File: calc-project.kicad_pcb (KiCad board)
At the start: 2 copper layers, 54 parts, among them J2 Conn_01x08_Socket, J3 Conn_01x08_Socket, J4 Conn_01x08_Socket, SW1 SW_Push_45deg, SW10 SW_Push_45deg, SW11 SW_Push_45deg, SW12 SW_Push_45deg, SW13 SW_Push_45deg, SW14 SW_Push_45deg, SW15 SW_Push_45deg, SW16 SW_Push_45deg, SW17 SW_Push_45deg, SW18 SW_Push_45deg, SW19 SW_Push_45deg, SW2 SW_Push_45deg, SW20 SW_Push_45deg, SW21 SW_Push_45deg, SW22 SW_Push_45deg, SW23 SW_Push_45deg, SW24 SW_Push_45deg, SW25 SW_Push_45deg, SW26 SW_Push_45deg, SW27 SW_Push_45deg, SW28 SW_Push_45deg, SW29 SW_Push_45deg, SW3 SW_Push_45deg, SW30 SW_Push_45deg, SW31 SW_Push_45deg, SW32 SW_Push_45deg, SW33 SW_Push_45deg, SW34 SW_Push_45deg, SW35 SW_Push_45deg, SW36 SW_Push_45deg, SW37 SW_Push_45deg, SW38 SW_Push_45deg, SW39 SW_Push_45deg, SW4 SW_Push_45deg, SW40 SW_Push_45deg, SW41 SW_Push_45deg, SW42 SW_Push_45deg, SW43 SW_Push_45deg, SW44 SW_Push_45deg, SW45 SW_Push_45deg, SW46 SW_Push_45deg, SW47 SW_Push_45deg, SW48 SW_Push_45deg, SW5 SW_Push_45deg, SW6 SW_Push_45deg, SW7 SW_Push_45deg, SW8 SW_Push_45deg, SW9 SW_Push_45deg

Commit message: added rpi pico, took away connectors, idk what else
idk what i did
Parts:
- added J1: PinSocket_1x20_Right, Connector_PinSocket_2.54mm:PinSocket_1x20_P2.54mm_Vertical_SMD_Pin1Left, B.Cu at (62.9, 68.0)
- added J2: PinSocket_1x20_Left, Connector_PinSocket_2.54mm:PinSocket_1x20_P2.54mm_Vertical_SMD_Pin1Left, B.Cu at (55.6, 68.0)
- moved SW43 76.2 mm to (133.0, 138.0), turned to 90 degrees
- moved SW48 75.6 mm to (133.0, 88.0), turned to 90 degrees
- moved SW44 70.7 mm to (133.0, 128.0), turned to 90 degrees
- moved SW47 70.2 mm to (133.0, 98.0), turned to 90 degrees
- moved SW45 67.6 mm to (133.0, 118.0), turned to 90 degrees
- moved SW46 67.5 mm to (133.0, 108.0), turned to 90 degrees
- moved SW37 65.3 mm to (124.0, 138.0), turned to 90 degrees
- moved SW42 64.5 mm to (124.0, 88.0), turned to 90 degrees
- moved J2 58.7 mm to (101.0, 74.0), turned to 90 degrees
- moved SW38 58.7 mm to (124.0, 128.0), turned to 90 degrees
- moved SW41 58.2 mm to (124.0, 98.0), turned to 90 degrees
- moved SW39 55.0 mm to (124.0, 118.0), turned to 90 degrees
- moved SW40 54.8 mm to (124.0, 108.0), turned to 90 degrees
- moved SW31 54.1 mm to (114.0, 138.0), turned to 90 degrees
- moved SW36 53.2 mm to (114.0, 88.0), turned to 90 degrees
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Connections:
- LCD1 pad 10: Net-(J3-Pin_4) -> unconnected-(LCD1-~{CSX}-Pad10)
- LCD1 pad 11: Net-(J3-Pin_3) -> unconnected-(LCD1-DCX-Pad11)
- LCD1 pad 12: Net-(J3-Pin_2) -> unconnected-(LCD1-WRX-Pad12)
- LCD1 pad 33: Net-(J3-Pin_1) -> unconnected-(LCD1-SDA-Pad33)
- SW1 pad 1: Net-(J4-Pin_8) -> Net-(SW1-Pad1)
- SW1 pad 2: Net-(J2-Pin_8) -> Net-(SW1-Pad2)
- SW10 pad 1: Net-(J4-Pin_5) -> Net-(SW10-Pad1)
- SW10 pad 2: Net-(J2-Pin_7) -> Net-(SW10-Pad2)
- SW11 pad 1: Net-(J4-Pin_4) -> Net-(SW11-Pad1)
- SW11 pad 2: Net-(J2-Pin_7) -> Net-(SW10-Pad2)
- SW12 pad 1: Net-(J4-Pin_3) -> Net-(SW12-Pad1)
- SW12 pad 2: Net-(J2-Pin_7) -> Net-(SW10-Pad2)
- SW13 pad 1: Net-(J4-Pin_8) -> Net-(SW1-Pad1)
- SW13 pad 2: Net-(J2-Pin_6) -> Net-(SW13-Pad2)
- SW14 pad 1: Net-(J4-Pin_7) -> Net-(SW14-Pad1)
- SW14 pad 2: Net-(J2-Pin_6) -> Net-(SW13-Pad2)
- SW15 pad 1: Net-(J4-Pin_6) -> Net-(SW15-Pad1)
- SW15 pad 2: Net-(J2-Pin_6) -> Net-(SW13-Pad2)
- SW16 pad 1: Net-(J4-Pin_5) -> Net-(SW10-Pad1)
- SW16 pad 2: Net-(J2-Pin_6) -> Net-(SW13-Pad2)
- SW17 pad 1: Net-(J4-Pin_4) -> Net-(SW11-Pad1)
- SW17 pad 2: Net-(J2-Pin_6) -> Net-(SW13-Pad2)
- SW18 pad 1: Net-(J4-Pin_3) -> Net-(SW12-Pad1)
- SW18 pad 2: Net-(J2-Pin_6) -> Net-(SW13-Pad2)
- SW19 pad 1: Net-(J4-Pin_8) -> Net-(SW1-Pad1)
- SW19 pad 2: Net-(J2-Pin_5) -> Net-(SW19-Pad2)
- SW2 pad 1: Net-(J4-Pin_7) -> Net-(SW14-Pad1)
- SW2 pad 2: Net-(J2-Pin_8) -> Net-(SW1-Pad2)
- SW20 pad 1: Net-(J4-Pin_7) -> Net-(SW14-Pad1)
- SW20 pad 2: Net-(J2-Pin_5) -> Net-(SW19-Pad2)
- SW21 pad 1: Net-(J4-Pin_6) -> Net-(SW15-Pad1)
- SW21 pad 2: Net-(J2-Pin_5) -> Net-(SW19-Pad2)
- SW22 pad 1: Net-(J4-Pin_5) -> Net-(SW10-Pad1)
- SW22 pad 2: Net-(J2-Pin_5) -> Net-(SW19-Pad2)
- SW23 pad 1: Net-(J4-Pin_4) -> Net-(SW11-Pad1)
- SW23 pad 2: Net-(J2-Pin_5) -> Net-(SW19-Pad2)
- SW24 pad 1: Net-(J4-Pin_3) -> Net-(SW12-Pad1)
- SW24 pad 2: Net-(J2-Pin_5) -> Net-(SW19-Pad2)
- SW25 pad 1: Net-(J4-Pin_8) -> Net-(SW1-Pad1)
- SW25 pad 2: Net-(J2-Pin_4) -> Net-(SW25-Pad2)
- SW26 pad 1: Net-(J4-Pin_7) -> Net-(SW14-Pad1)
- SW26 pad 2: Net-(J2-Pin_4) -> Net-(SW25-Pad2)
- SW27 pad 1: Net-(J4-Pin_6) -> Net-(SW15-Pad1)
- SW27 pad 2: Net-(J2-Pin_4) -> Net-(SW25-Pad2)
- SW28 pad 1: Net-(J4-Pin_5) -> Net-(SW10-Pad1)
- SW28 pad 2: Net-(J2-Pin_4) -> Net-(SW25-Pad2)
- SW29 pad 1: Net-(J4-Pin_4) -> Net-(SW11-Pad1)
- SW29 pad 2: Net-(J2-Pin_4) -> Net-(SW25-Pad2)
- SW3 pad 1: Net-(J4-Pin_6) -> Net-(SW15-Pad1)
- SW3 pad 2: Net-(J2-Pin_8) -> Net-(SW1-Pad2)
- SW30 pad 1: Net-(J4-Pin_3) -> Net-(SW12-Pad1)
- SW30 pad 2: Net-(J2-Pin_4) -> Net-(SW25-Pad2)
- SW31 pad 1: Net-(J4-Pin_8) -> Net-(SW1-Pad1)
- SW31 pad 2: Net-(J2-Pin_3) -> Net-(SW31-Pad2)
- SW32 pad 1: Net-(J4-Pin_7) -> Net-(SW14-Pad1)
- SW32 pad 2: Net-(J2-Pin_3) -> Net-(SW31-Pad2)
- SW33 pad 1: Net-(J4-Pin_6) -> Net-(SW15-Pad1)
- SW33 pad 2: Net-(J2-Pin_3) -> Net-(SW31-Pad2)
- SW34 pad 1: Net-(J4-Pin_5) -> Net-(SW10-Pad1)
- SW34 pad 2: Net-(J2-Pin_3) -> Net-(SW31-Pad2)
- SW35 pad 1: Net-(J4-Pin_4) -> Net-(SW11-Pad1)
- SW35 pad 2: Net-(J2-Pin_3) -> Net-(SW31-Pad2)
- SW36 pad 1: Net-(J4-Pin_3) -> Net-(SW12-Pad1)
- SW36 pad 2: Net-(J2-Pin_3) -> Net-(SW31-Pad2)
- SW37 pad 1: Net-(J4-Pin_8) -> Net-(SW1-Pad1)
- SW37 pad 2: Net-(J2-Pin_2) -> Net-(SW37-Pad2)
- SW38 pad 1: Net-(J4-Pin_7) -> Net-(SW14-Pad1)
- SW38 pad 2: Net-(J2-Pin_2) -> Net-(SW37-Pad2)
- SW39 pad 1: Net-(J4-Pin_6) -> Net-(SW15-Pad1)
- SW39 pad 2: Net-(J2-Pin_2) -> Net-(SW37-Pad2)
- SW4 pad 1: Net-(J4-Pin_5) -> Net-(SW10-Pad1)
- SW4 pad 2: Net-(J2-Pin_8) -> Net-(SW1-Pad2)
- SW40 pad 1: Net-(J4-Pin_5) -> Net-(SW10-Pad1)
- SW40 pad 2: Net-(J2-Pin_2) -> Net-(SW37-Pad2)
- SW41 pad 1: Net-(J4-Pin_4) -> Net-(SW11-Pad1)
- SW41 pad 2: Net-(J2-Pin_2) -> Net-(SW37-Pad2)
- SW42 pad 1: Net-(J4-Pin_3) -> Net-(SW12-Pad1)
- SW42 pad 2: Net-(J2-Pin_2) -> Net-(SW37-Pad2)
- SW43 pad 1: Net-(J4-Pin_8) -> Net-(SW1-Pad1)
- SW43 pad 2: Net-(J2-Pin_1) -> Net-(SW43-Pad2)
- SW44 pad 1: Net-(J4-Pin_7) -> Net-(SW14-Pad1)
- SW44 pad 2: Net-(J2-Pin_1) -> Net-(SW43-Pad2)
- SW45 pad 1: Net-(J4-Pin_6) -> Net-(SW15-Pad1)
- SW45 pad 2: Net-(J2-Pin_1) -> Net-(SW43-Pad2)
- SW46 pad 1: Net-(J4-Pin_5) -> Net-(SW10-Pad1)
- SW46 pad 2: Net-(J2-Pin_1) -> Net-(SW43-Pad2)
- SW47 pad 1: Net-(J4-Pin_4) -> Net-(SW11-Pad1)
- SW47 pad 2: Net-(J2-Pin_1) -> Net-(SW43-Pad2)
- SW48 pad 1: Net-(J4-Pin_3) -> Net-(SW12-Pad1)
- SW48 pad 2: Net-(J2-Pin_1) -> Net-(SW43-Pad2)
- SW5 pad 1: Net-(J4-Pin_4) -> Net-(SW11-Pad1)
- SW5 pad 2: Net-(J2-Pin_8) -> Net-(SW1-Pad2)
- SW6 pad 1: Net-(J4-Pin_3) -> Net-(SW12-Pad1)
- SW6 pad 2: Net-(J2-Pin_8) -> Net-(SW1-Pad2)
- SW7 pad 1: Net-(J4-Pin_8) -> Net-(SW1-Pad1)
- SW7 pad 2: Net-(J2-Pin_7) -> Net-(SW10-Pad2)
- SW8 pad 1: Net-(J4-Pin_7) -> Net-(SW14-Pad1)
- SW8 pad 2: Net-(J2-Pin_7) -> Net-(SW10-Pad2)
- SW9 pad 1: Net-(J4-Pin_6) -> Net-(SW15-Pad1)
- SW9 pad 2: Net-(J2-Pin_7) -> Net-(SW10-Pad2)

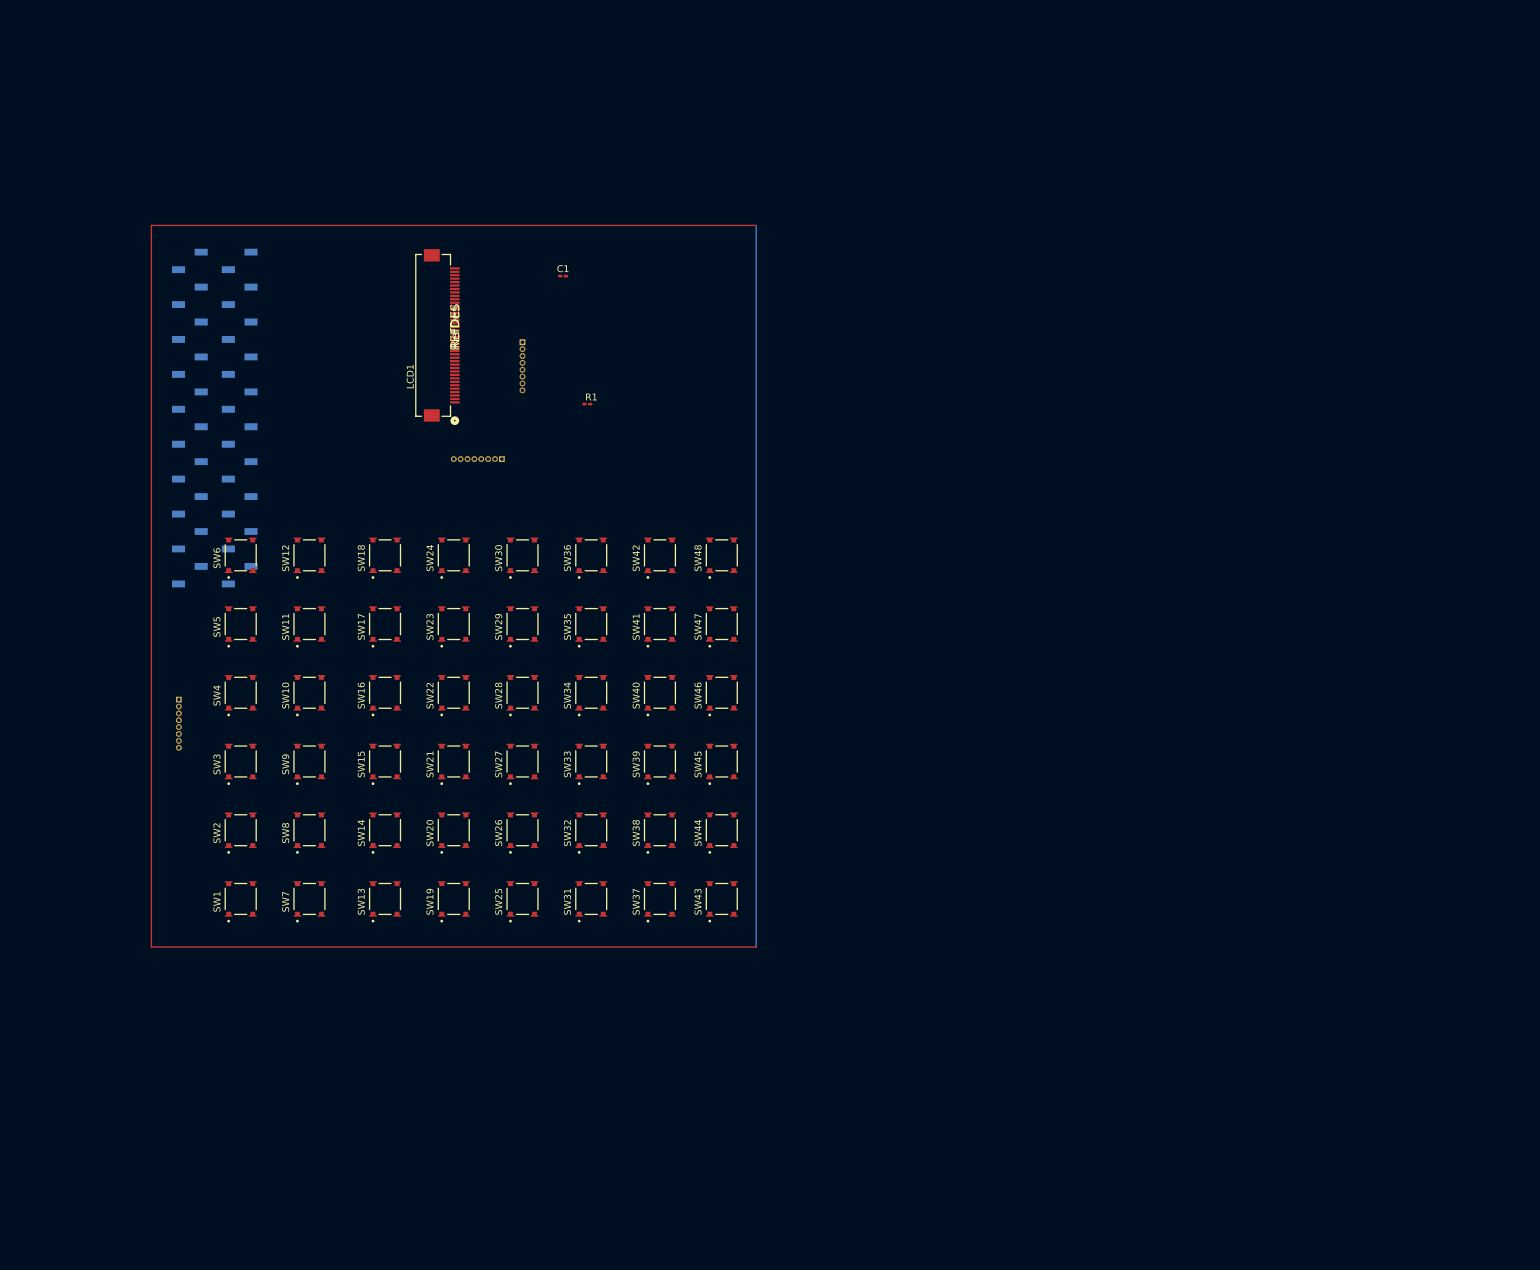
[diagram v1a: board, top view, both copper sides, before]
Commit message: we're now setting ourselves up for new screen, still need alignment
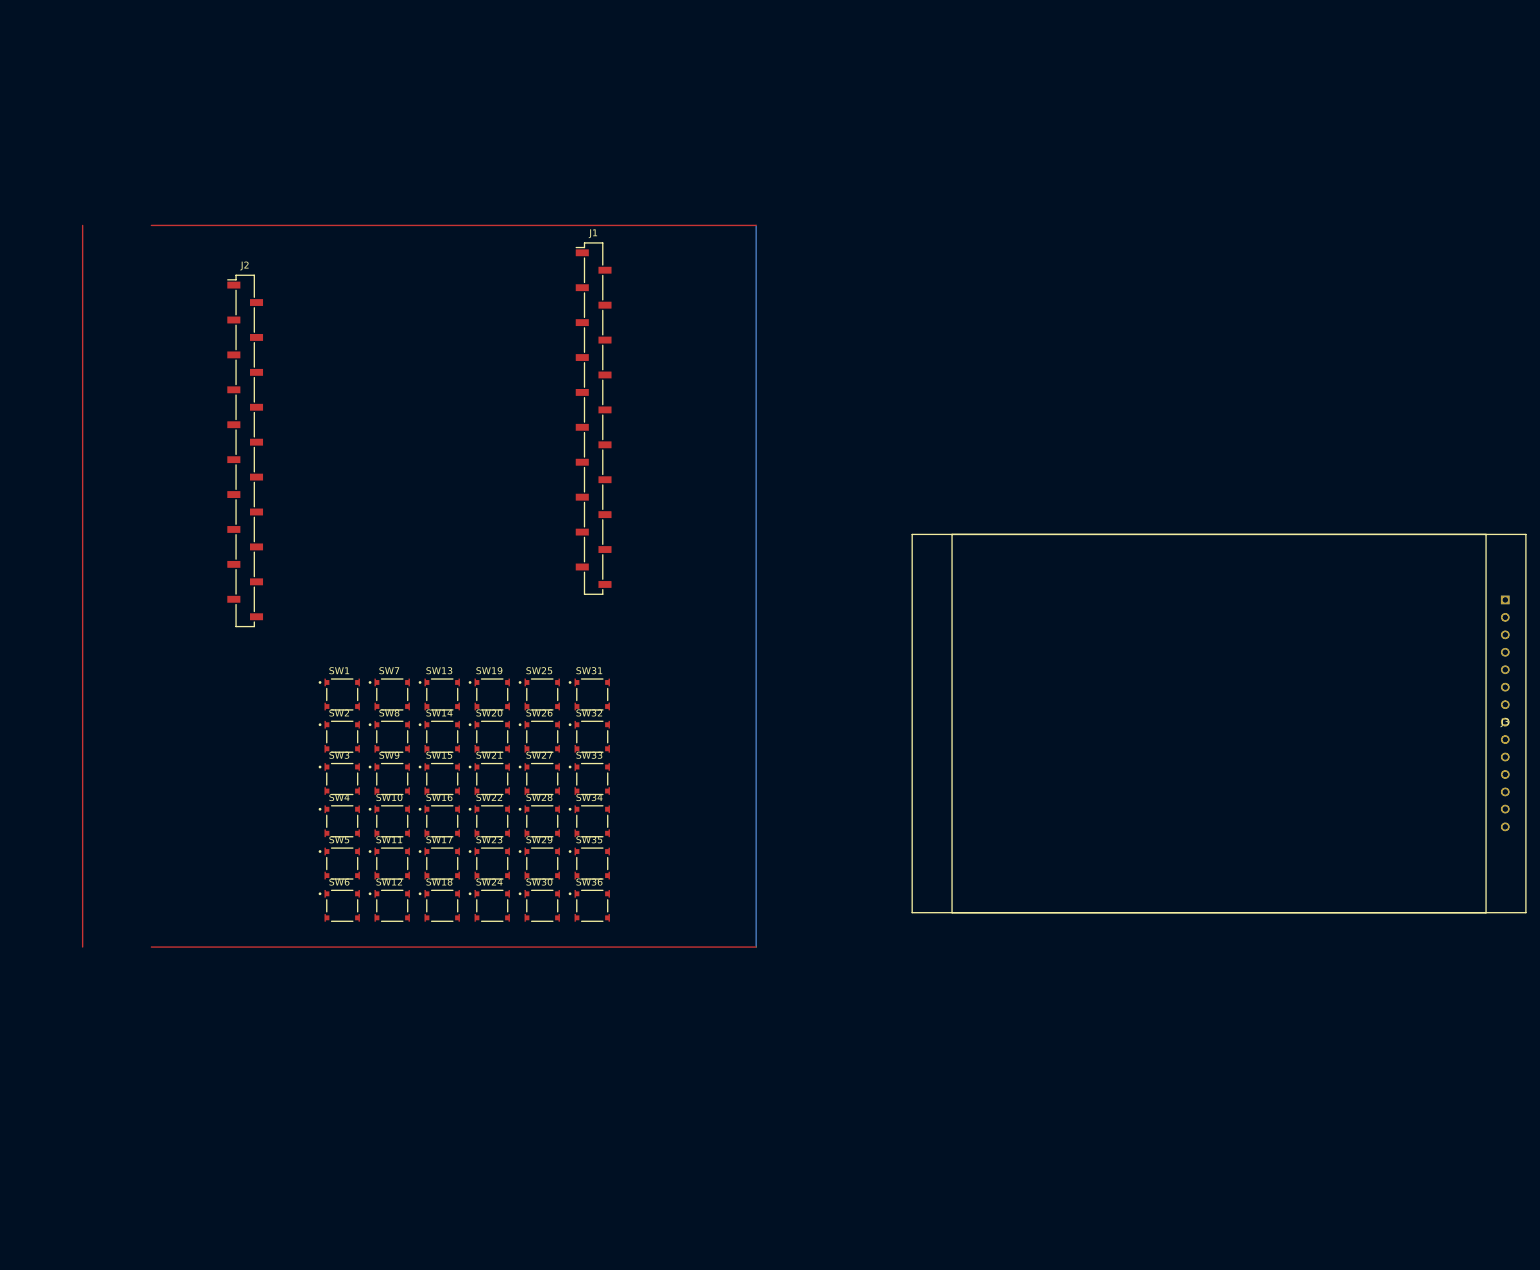
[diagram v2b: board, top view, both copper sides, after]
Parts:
- removed C1: 100nF, Capacitor_SMD:C_0201_0603Metric_Pad0.64x0.40mm_HandSolder
- removed the J2 at (101.0, 74.0)
- removed the J2 at (55.6, 68.0)
- removed J4: Conn_01x08_Socket, Connector_PinSocket_1.00mm:PinSocket_1x08_P1.00mm_Vertical
- removed LCD1: E28GA-T-CW250-N, Library:CONN40_FH12S-40S_HIR
- removed R1: 100, Resistor_SMD:R_0201_0603Metric_Pad0.64x0.40mm_HandSolder
- removed SW37, SW38, SW39, SW40, SW41, SW42, SW43, SW44, SW45, SW46, SW47, SW48: SW_Push_45deg, Library:SW_TL3315NF160Q
- added J2: PinSocket_1x20_Left, Connector_PinSocket_2.54mm:PinSocket_1x20_P2.54mm_Vertical_SMD_Pin1Left, F.Cu at (63.6, 72.8)
- J1: moved to F.Cu
- J3: value Conn_01x08_Socket -> Conn_01x14; footprint Connector_PinSocket_1.00mm:PinSocket_1x08_P1.00mm_Vertical -> Library:castel_toScreen; moved to F.Cu
- moved J3 152.9 mm to (247.0, 111.0), turned to 0 degrees
- moved SW6 53.1 mm to (77.8, 139.0), turned to 0 degrees
- moved SW12 52.4 mm to (85.0, 139.0), turned to 0 degrees
- moved SW18 51.7 mm to (92.3, 139.0), turned to 0 degrees
- moved J1 51.5 mm to (114.3, 68.1), turned to 0 degrees
- moved SW24 51.3 mm to (99.6, 139.0), turned to 0 degrees
- moved SW30 51.1 mm to (106.9, 139.0), turned to 0 degrees
- moved SW36 51.0 mm to (114.2, 139.0), turned to 0 degrees
- moved SW5 37.9 mm to (77.8, 132.8), turned to 0 degrees
- moved SW11 36.9 mm to (85.0, 132.8), turned to 0 degrees
- moved SW17 35.8 mm to (92.3, 132.8), turned to 0 degrees
- moved SW23 35.3 mm to (99.6, 132.8), turned to 0 degrees
- moved SW29 35.0 mm to (106.9, 132.8), turned to 0 degrees
- moved SW35 34.9 mm to (114.2, 132.8), turned to 0 degrees
- moved SW1 33.2 mm to (77.8, 108.2), turned to 0 degrees
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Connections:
- net Net-(SW1-Pad1) renamed col 5
- net Net-(SW1-Pad2) renamed row 0
- net Net-(SW10-Pad1) renamed col 2
- net Net-(SW10-Pad2) renamed row 1
- net Net-(SW11-Pad1) renamed col 1
- net Net-(SW12-Pad1) renamed col 0
- net Net-(SW13-Pad2) renamed row 2
- net Net-(SW14-Pad1) renamed col 4
- net Net-(SW15-Pad1) renamed col 3
- net Net-(SW19-Pad2) renamed row 3
- net Net-(SW25-Pad2) renamed row 4
- net Net-(SW31-Pad2) renamed row 5
- J3 pad 1: Net-(J3-Pin_1) -> +3.3V
- J3 pad 2: Net-(J3-Pin_2) -> GND
- J3 pad 3: Net-(J3-Pin_3) -> Chip select
- J3 pad 4: Net-(J3-Pin_4) -> RESET
- J3 pad 5: unconnected-(J3-Pin_5-Pad5) -> Data/Comm select
- J3 pad 6: unconnected-(J3-Pin_6-Pad6) -> DISPLAY_DATA_IN
- J3 pad 7: +3.3V -> Write strobe sig
- J3 pad 8: GND -> LED_CTRL

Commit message: fixed names, seems like schematic is good
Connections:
- net Chip select renamed CS
- net DISPLAY_DATA_IN renamed SDI(MOSI)
- net Data/Comm select renamed DC_SELECT
- net Write strobe sig renamed SCK
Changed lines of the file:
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@@
 			(size 1.9 1)
 			(layers "F.Cu" "F.Mask" "F.Paste")
-			(net "Data{slash}Comm select")
+			(net "DC_SELECT")
 			(pinfunction "GP16_21")
 			(pintype "passive")
@@
 			(size 1.9 1)
 			(layers "F.Cu" "F.Mask" "F.Paste")
-			(net "Chip select")
+			(net "CS")
 			(pinfunction "GP17_22")
 			(pintype "passive")
@@
 			(size 1.9 1)
 			(layers "F.Cu" "F.Mask" "F.Paste")
-			(net "Write strobe sig")
+			(net "SCK")
 			(pinfunction "GP18_24")
 			(pintype "passive")
@@
 			(size 1.9 1)
 			(layers "F.Cu" "F.Mask" "F.Paste")
-			(net "DISPLAY_DATA_IN")
+			(net "SDI(MOSI)")
 			(pinfunction "GP19_25")
 			(pintype "passive")
@@
 		(sheetname "/")
 		(sheetfile "calc-project.kicad_sch")
+		(units
+			(unit
+				(name "A")
+				(pins "1" "2" "3" "4" "5" "6" "7" "8" "9" "10" "11" "12" "13" "14")
+			)
+		)
 		(attr smd)
 		(duplicate_pad_numbers_are_jumpers no)
@@
 			(layers "*.Cu" "*.Mask")
 			(remove_unused_layers no)
-			(net "Chip select")
+			(net "CS")
 			(pinfunction "Pin_3_3")
 			(pintype "passive")
@@
 			(layers "*.Cu" "*.Mask")
 			(remove_unused_layers no)
-			(net "Data{slash}Comm select")
+			(net "DC_SELECT")
 			(pinfunction "Pin_5_5")
 			(pintype "passive")
@@
 			(layers "*.Cu" "*.Mask")
 			(remove_unused_layers no)
-			(net "DISPLAY_DATA_IN")
+			(net "SDI(MOSI)")
 			(pinfunction "Pin_6_6")
 			(pintype "passive")
@@
 			(layers "*.Cu" "*.Mask")
 			(remove_unused_layers no)
-			(net "Write strobe sig")
+			(net "SCK")
 			(pinfunction "Pin_7_7")
 			(pintype "passive")
